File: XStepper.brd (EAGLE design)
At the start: 100.3 x 80 mm, 74 parts, among them Q2 16 MHZ

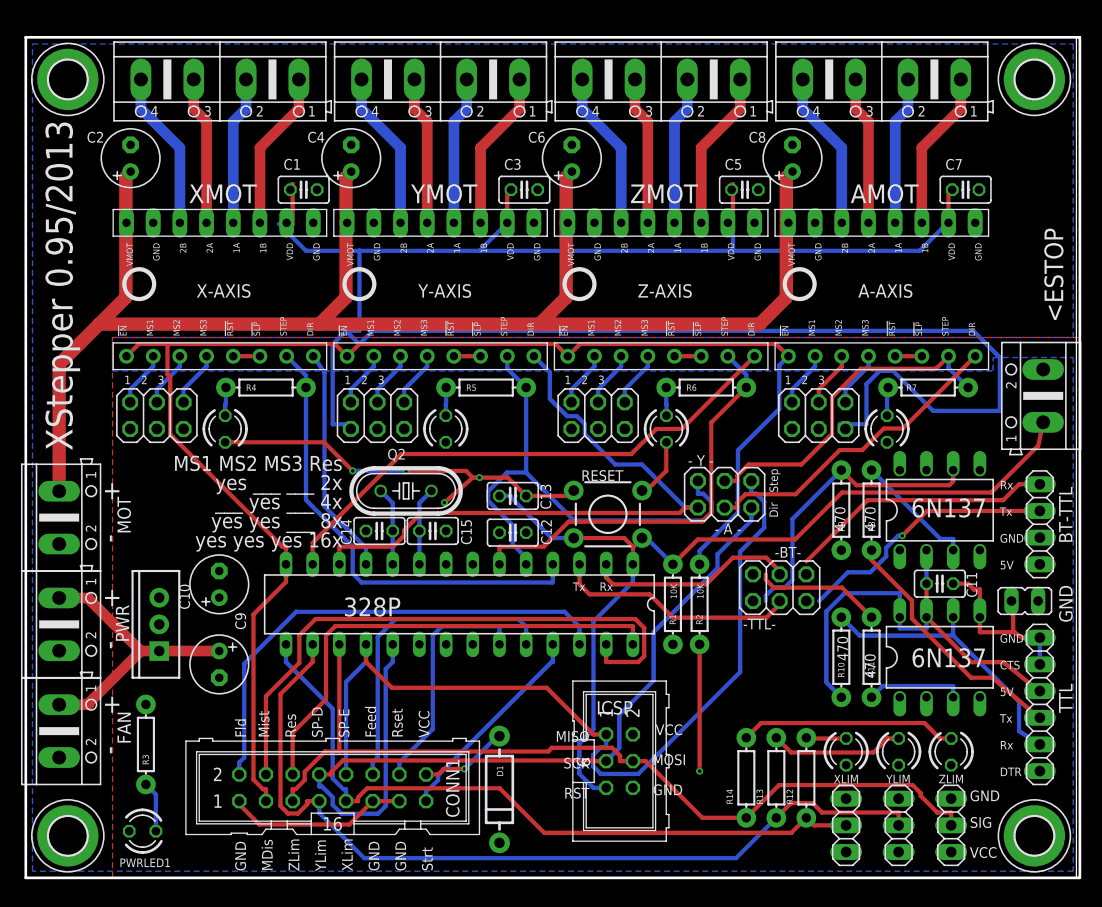
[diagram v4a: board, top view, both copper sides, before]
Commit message: - bugfix diode
- add new autorouting
- move emergency screw near to cpu
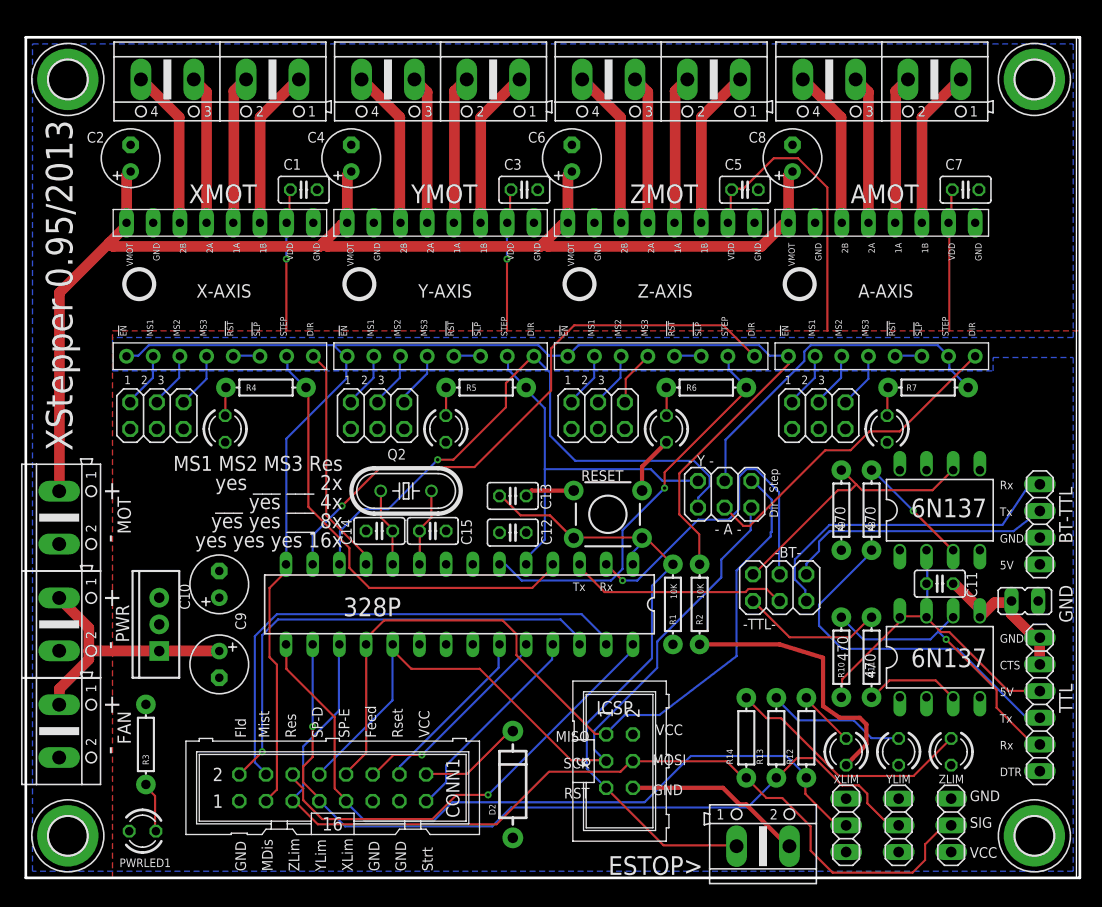
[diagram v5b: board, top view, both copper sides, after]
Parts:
- removed <ESTOP: (no value), con-ptr500:AK500/2
- removed D1: (no value), SparkFun-DiscreteSemi:DIODE-1N4001
- added D2: (no value), SparkFun-DiscreteSemi:DIODE-1N4001
- added ESTOP>: (no value), con-ptr500:AK500/2
- moved R12 3.81 mm to (74.3, 13.3)
- moved R13 3.81 mm to (71.4, 13.3)
- moved R14 3.81 mm to (68.6, 13.3)
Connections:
- net 5V: now also D2.A; no longer D1.C
- net GND: now also ESTOP>.2; no longer <ESTOP.2
- net N$45: now also D2.C; no longer D1.A
- net RESET: now also ESTOP>.1; no longer <ESTOP.1
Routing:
- net 5V: track 201.2 -> 69.5 mm, vias 0 -> 2
- net RESET: track 88.5 -> 62.3 mm
- net PWRMOT: track 144.0 -> 120.6 mm
- net GND: track 74.4 -> 53.2 mm, vias 5 -> 0
- net RXD: track 19.9 -> 32.1 mm, vias 0 -> 1
- net SPINDLE-DIR: track 82.8 -> 71.4 mm
- net Y-STEP: track 48.3 -> 37.1 mm
- net FEED-HOLD: track 30.1 -> 20.1 mm, vias 0 -> 1
- net USB_TXD: track 24.0 -> 33.9 mm
- net USB_5V: track 43.4 -> 33.5 mm
- net Z-STOP: track 82.9 -> 91.4 mm
- net COOLANT-MIST: track 56.6 -> 49.4 mm
- net G-RESET: track 23.0 -> 16.4 mm
- net BTTXD: track 25.3 -> 31.2 mm
- net SPINDLE-ENABLE: track 82.6 -> 77.2 mm
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
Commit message: - add VMOT sign to driver for users
- remove circle for pod cuz they are different on drivers
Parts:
- R12, R13, R14: value (none) -> 220
- R3: value (none) -> 330
- R4, R5, R6, R7: value (none) -> 110
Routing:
- net PWRMOT: track 120.6 -> 127.9 mm
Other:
- board text added: "VMOT>"
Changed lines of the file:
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@@
 <text x="52.07" y="27.305" size="0.8128" layer="25">Tx</text>
 <text x="54.61" y="27.305" size="0.8128" layer="25">Rx</text>
-<circle x="10.795" y="56.515" radius="1.419903125" width="0.4064" layer="25"/>
-<circle x="31.75" y="56.515" radius="1.419903125" width="0.4064" layer="25"/>
-<circle x="52.705" y="56.515" radius="1.419903125" width="0.4064" layer="25"/>
-<circle x="73.66" y="56.515" radius="1.419903125" width="0.4064" layer="25"/>
+<text x="8.89" y="55.245" size="1.27" layer="25" font="vector" rot="R90">VMOT&gt;</text>
+<text x="29.845" y="55.245" size="1.27" layer="25" font="vector" rot="R90">VMOT&gt;</text>
+<text x="50.8" y="55.245" size="1.27" layer="25" font="vector" rot="R90">VMOT&gt;</text>
+<text x="71.755" y="55.245" size="1.27" layer="25" font="vector" rot="R90">VMOT&gt;</text>
 </plain>
 <attributes>
@@
 </element>
 <element name="IC1" library="SparkFun-PowerIC" package="TO220-IGO" value="" x="12.7" y="24.13" rot="R90"/>
-<element name="R3" library="SparkFun-Resistors" package="AXIAL-0.3" value="" x="11.43" y="12.7" smashed="yes" rot="R270">
+<element name="R3" library="SparkFun-Resistors" package="AXIAL-0.3" value="330" x="11.43" y="12.7" smashed="yes" rot="R270">
 <attribute name="NAME" x="11.1125" y="11.7475" size="0.6096" layer="25" font="vector" rot="R270"/>
 <attribute name="VALUE" x="11.049" y="14.732" size="1.016" layer="21" font="vector" ratio="15" rot="R270"/>
@@
 <attribute name="VALUE" x="64.516" y="26.543" size="0.6096" layer="21" font="vector" ratio="15" rot="R90"/>
 </element>
-<element name="R4" library="SparkFun-Resistors" package="AXIAL-0.3" value="" x="22.8601" y="46.6725" smashed="yes">
+<element name="R4" library="SparkFun-Resistors" package="AXIAL-0.3" value="110" x="22.8601" y="46.6725" smashed="yes">
 <attribute name="NAME" x="20.9551" y="46.355" size="0.6096" layer="25" font="vector"/>
 <attribute name="VALUE" x="20.8281" y="46.2915" size="1.016" layer="21" font="vector" ratio="15"/>
 </element>
-<element name="R5" library="SparkFun-Resistors" package="AXIAL-0.3" value="" x="43.8151" y="46.6725" smashed="yes">
+<element name="R5" library="SparkFun-Resistors" package="AXIAL-0.3" value="110" x="43.8151" y="46.6725" smashed="yes">
 <attribute name="NAME" x="41.9101" y="46.355" size="0.6096" layer="25" font="vector"/>
 <attribute name="VALUE" x="41.7831" y="46.2915" size="1.016" layer="21" font="vector" ratio="15"/>
 </element>
-<element name="R6" library="SparkFun-Resistors" package="AXIAL-0.3" value="" x="64.7701" y="46.6725" smashed="yes">
+<element name="R6" library="SparkFun-Resistors" package="AXIAL-0.3" value="110" x="64.7701" y="46.6725" smashed="yes">
 <attribute name="NAME" x="62.8651" y="46.355" size="0.6096" layer="25" font="vector"/>
 <attribute name="VALUE" x="62.7381" y="46.2915" size="1.016" layer="21" font="vector" ratio="15"/>
 </element>
-<element name="R7" library="SparkFun-Resistors" package="AXIAL-0.3" value="" x="85.8838" y="46.6725" smashed="yes">
+<element name="R7" library="SparkFun-Resistors" package="AXIAL-0.3" value="110" x="85.8838" y="46.6725" smashed="yes">
 <attribute name="NAME" x="83.82005" y="46.355" size="0.6096" layer="25" font="vector"/>
 <attribute name="VALUE" x="83.8518" y="46.2915" size="1.016" layer="21" font="vector" ratio="15"/>
 </element>
-<element name="R12" library="SparkFun-Resistors" package="AXIAL-0.3" value="" x="74.295" y="13.335" smashed="yes" rot="R90">
+<element name="R12" library="SparkFun-Resistors" package="AXIAL-0.3" value="220" x="74.295" y="13.335" smashed="yes" rot="R90">
 <attribute name="NAME" x="73.025" y="10.795" size="0.6096" layer="25" font="vector" rot="R90"/>
 <attribute name="VALUE" x="74.676" y="11.303" size="1.016" layer="21" font="vector" ratio="15" rot="R90"/>
 </element>
-<element name="R13" library="SparkFun-Resistors" package="AXIAL-0.3" value="" x="71.4375" y="13.335" smashed="yes" rot="R90">
+<element name="R13" library="SparkFun-Resistors" package="AXIAL-0.3" value="220" x="71.4375" y="13.335" smashed="yes" rot="R90">
 <attribute name="NAME" x="70.1675" y="10.795" size="0.6096" layer="25" font="vector" rot="R90"/>
 <attribute name="VALUE" x="71.8185" y="11.303" size="1.016" layer="21" font="vector" ratio="15" rot="R90"/>
 </element>
-<element name="R14" library="SparkFun-Resistors" package="AXIAL-0.3" value="" x="68.58" y="13.335" smashed="yes" rot="R90">
+<element name="R14" library="SparkFun-Resistors" package="AXIAL-0.3" value="220" x="68.58" y="13.335" smashed="yes" rot="R90">
 <attribute name="NAME" x="67.31" y="10.795" size="0.6096" layer="25" font="vector" rot="R90"/>
 <attribute name="VALUE" x="68.961" y="11.303" size="1.016" layer="21" font="vector" ratio="15" rot="R90"/>
@@
 <wire x1="67.945" y1="6.985" x2="68.58" y2="6.985" width="0.4064" layer="1"/>
 <wire x1="68.58" y1="6.985" x2="72.39" y2="3.175" width="0.4064" layer="1"/>
-<wire x1="64.135" y1="22.225" x2="71.755" y2="22.225" width="0.4064" layer="1"/>
+<wire x1="64.135" y1="22.225" x2="65.405" y2="20.955" width="0.4064" layer="1"/>
 <wire x1="78.08" y1="10.73" x2="80.01" y2="12.7" width="0.4064" layer="1"/>
 <wire x1="80.01" y1="12.7" x2="80.01" y2="14.605" width="0.4064" layer="1"/>
 <wire x1="80.01" y1="14.605" x2="79.375" y2="15.24" width="0.4064" layer="1"/>
-<wire x1="79.375" y1="15.24" x2="77.47" y2="15.24" width="0.4064" layer="1"/>
-<wire x1="77.47" y1="15.24" x2="75.8825" y2="16.35125" width="0.4064" layer="1"/>
+<wire x1="79.375" y1="15.24" x2="76.99375" y2="15.24" width="0.4064" layer="1"/>
+<wire x1="76.99375" y1="15.24" x2="75.8825" y2="16.35125" width="0.4064" layer="1"/>
 <wire x1="75.8825" y1="16.35125" x2="75.8825" y2="20.955" width="0.4064" layer="1"/>
-<wire x1="75.8825" y1="20.955" x2="71.755" y2="22.225" width="0.4064" layer="1"/>
+<wire x1="75.8825" y1="20.955" x2="65.405" y2="20.955" width="0.4064" layer="1"/>
 </signal>
 <signal name="N$5">
@@
 <wire x1="25.1" y1="65.5" x2="25.1825" y2="65.5" width="0.2032" layer="1"/>
 <wire x1="24.9" y1="62.4" x2="24.8263" y2="62.35" width="0.2032" layer="1"/>
-<wire x1="24.8" y1="58.9" x2="24.8" y2="62.3" width="0.2032" layer="16"/>
-<wire x1="24.8" y1="52.07" x2="24.8" y2="58.9" width="0.2032" layer="1"/>
+<wire x1="24.8" y1="55.725" x2="24.8" y2="62.3" width="0.2032" layer="16"/>
+<wire x1="24.8" y1="52.07" x2="24.8" y2="55.725" width="0.2032" layer="1"/>
 <wire x1="24.8" y1="62.3" x2="24.8263" y2="62.35" width="0.2032" layer="16"/>
-<wire x1="45.8" y1="58.9" x2="45.8" y2="62.3" width="0.2032" layer="16"/>
-<wire x1="45.8" y1="52.07" x2="45.8" y2="58.9" width="0.2032" layer="1"/>
+<wire x1="45.8" y1="55.725" x2="45.8" y2="62.3" width="0.2032" layer="16"/>
+<wire x1="45.8" y1="52.07" x2="45.8" y2="55.725" width="0.2032" layer="1"/>
 <wire x1="45.8" y1="62.3" x2="45.8263" y2="62.35" width="0.2032" layer="16"/>
 <wire x1="68.3" y1="65.6" x2="67.2" y2="65.6" width="0.2032" layer="1"/>
@@
 <wire x1="87.9" y1="52.07" x2="87.9" y2="62.3" width="0.2032" layer="1"/>
 <wire x1="87.9" y1="62.3" x2="87.8262" y2="62.35" width="0.2032" layer="1"/>
-<via x="24.8" y="58.9" extent="1-16" drill="0.3302"/>
-<via x="45.8" y="58.9" extent="1-16" drill="0.3302"/>
+<via x="24.8" y="55.725" extent="1-16" drill="0.3302"/>
+<via x="45.8" y="55.725" extent="1-16" drill="0.3302"/>
 <wire x1="77.6" y1="31.2" x2="77.625" y2="31.19" width="0.2032" layer="1"/>
 </signal>
@@
 <wire x1="9.9" y1="67.2" x2="9.9763" y2="67.23" width="1.016" layer="1"/>
 <wire x1="3.2" y1="55.7" x2="3.2" y2="36.9" width="1.016" layer="1"/>
-<wire x1="9.4" y1="61.9" x2="7.95" y2="60.45" width="1.016" layer="1"/>
-<wire x1="7.95" y1="60.45" x2="3.2" y2="55.7" width="1.016" layer="1"/>
+<wire x1="9.4" y1="61.9" x2="6.045" y2="58.545" width="1.016" layer="1"/>
+<wire x1="6.045" y1="58.545" x2="3.2" y2="55.7" width="1.016" layer="1"/>
 <wire x1="3.2" y1="36.9" x2="3.175" y2="36.8046" width="1.016" layer="1"/>
 <wire x1="9.4" y1="61.9" x2="9.5863" y2="62.35" width="1.016" layer="1"/>
-<wire x1="28" y1="60.1" x2="28.35" y2="60.45" width="1.016" layer="1"/>
-<wire x1="28.35" y1="60.45" x2="30.1" y2="62.2" width="1.016" layer="1"/>
-<wire x1="8.3" y1="60.1" x2="28" y2="60.1" width="1.016" layer="1"/>
+<wire x1="27.52375" y1="58.195" x2="27.55625" y2="58.2275" width="1.016" layer="1"/>
+<wire x1="27.55625" y1="58.2275" x2="30.1" y2="62.2" width="1.016" layer="1"/>
+<wire x1="7.03" y1="58.195" x2="27.52375" y2="58.195" width="1.016" layer="1"/>
 <wire x1="30.1" y1="62.2" x2="30.5863" y2="62.35" width="1.016" layer="1"/>
-<wire x1="8.3" y1="60.1" x2="7.95" y2="60.45" width="1.016" layer="1"/>
-<wire x1="49" y1="60.1" x2="49.35" y2="60.45" width="1.016" layer="1"/>
-<wire x1="49.35" y1="60.45" x2="51.1" y2="62.2" width="1.016" layer="1"/>
-<wire x1="28.7" y1="60.1" x2="49" y2="60.1" width="1.016" layer="1"/>
+<wire x1="7.03" y1="58.195" x2="6.045" y2="58.545" width="1.016" layer="1"/>
+<wire x1="48.365" y1="58.195" x2="48.715" y2="58.545" width="1.016" layer="1"/>
+<wire x1="48.715" y1="58.545" x2="51.1" y2="62.2" width="1.016" layer="1"/>
+<wire x1="28.7" y1="58.195" x2="48.365" y2="58.195" width="1.016" layer="1"/>
 <wire x1="51.1" y1="62.2" x2="51.5863" y2="62.35" width="1.016" layer="1"/>
-<wire x1="28.7" y1="60.1" x2="28.35" y2="60.45" width="1.016" layer="1"/>
-<wire x1="70" y1="60.1" x2="72.1" y2="62.2" width="1.016" layer="1"/>
-<wire x1="49.7" y1="60.1" x2="70" y2="60.1" width="1.016" layer="1"/>
+<wire x1="28.7" y1="58.195" x2="27.55625" y2="58.2275" width="1.016" layer="1"/>
+<wire x1="68.73" y1="58.195" x2="72.1" y2="62.2" width="1.016" layer="1"/>
+<wire x1="48.43" y1="58.195" x2="68.73" y2="58.195" width="1.016" layer="1"/>
 <wire x1="72.1" y1="62.2" x2="72.5862" y2="62.35" width="1.016" layer="1"/>
-<wire x1="49.7" y1="60.1" x2="49.35" y2="60.45" width="1.016" layer="1"/>
+<wire x1="48.43" y1="58.195" x2="48.715" y2="58.545" width="1.016" layer="1"/>
 </signal>
 <signal name="N$43">

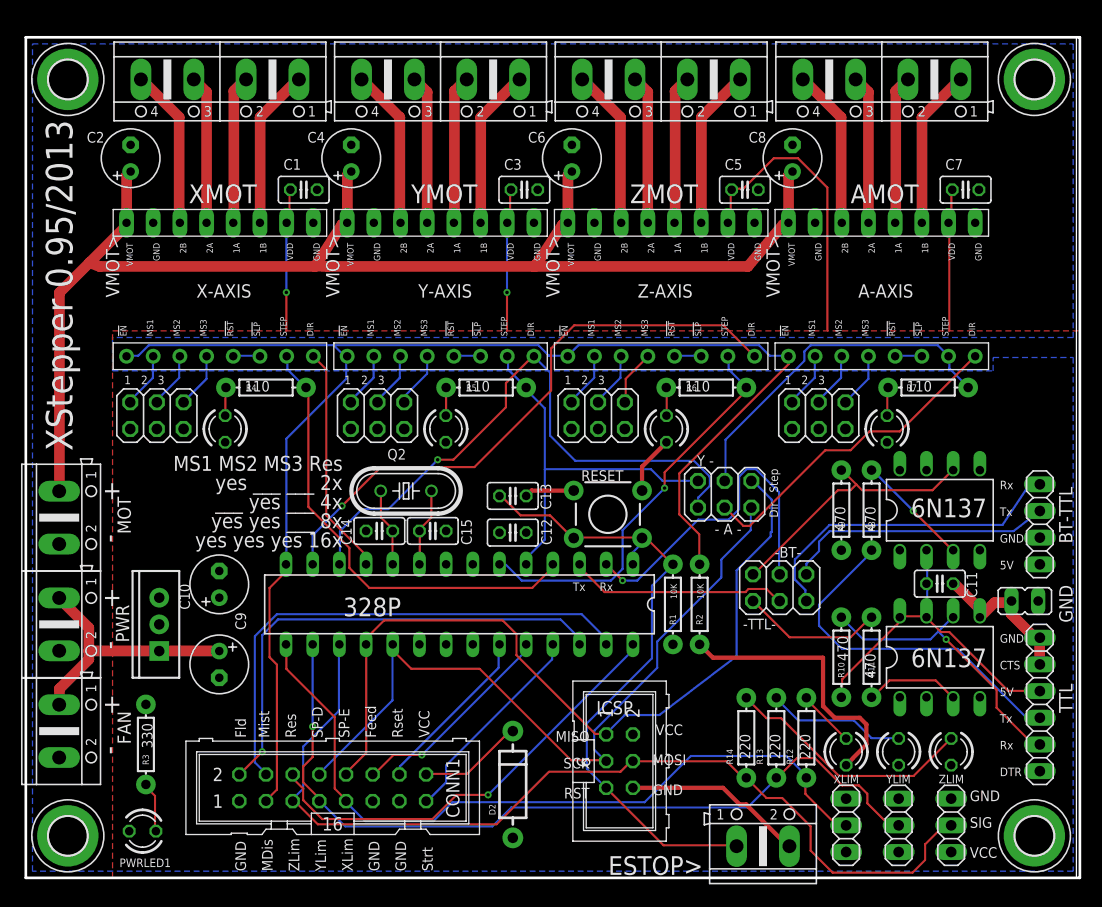
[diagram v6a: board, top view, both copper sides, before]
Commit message: - some changes for community
* move screw terminals for motors 1mm up for bigger caps
* add a 12V voltage regulator for fan
* replace powerled resitor to a small one
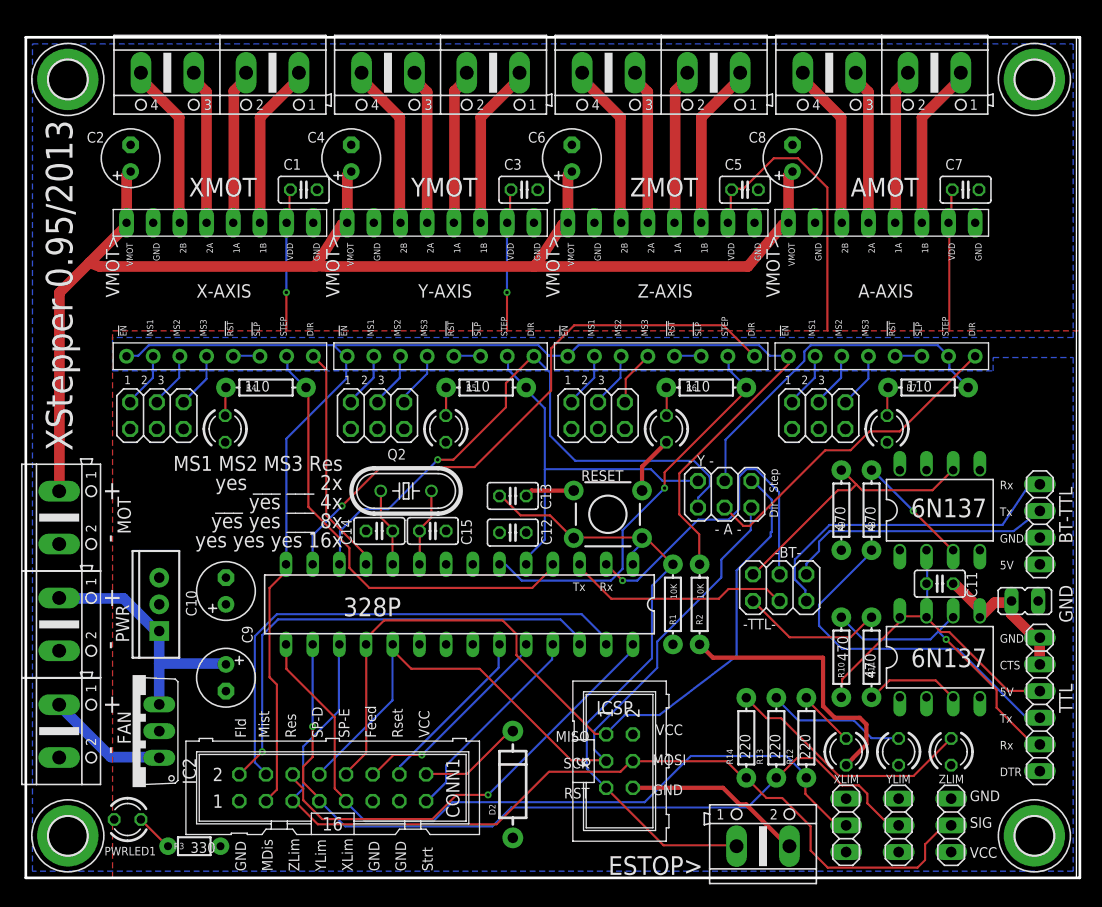
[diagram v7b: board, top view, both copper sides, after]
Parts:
- added IC2: 7812TV, linear:TO220V
- R3: device SparkFun-Resistors:AXIAL-0.3 -> SparkFun-Resistors:1/6W-RES
- moved R3 10.7 mm to (16.0, 3.02), turned to 180 degrees
- moved IC1 1.91 mm to (12.7, 26.0)
- moved PWRLED1 1.81 mm to (9.68, 5.56)
- moved C9 1.42 mm to (19.1, 19.1)
- moved C10 0.90 mm to (19.1, 27.3)
- moved AMOT 0.64 mm to (81.5, 76.6)
- moved XMOT 0.64 mm to (18.5, 76.6)
- moved YMOT 0.64 mm to (39.5, 76.6)
- moved ZMOT 0.64 mm to (60.5, 76.6)
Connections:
- new net N$46: FAN.1, IC2.1
- net 12V: now also IC2.3; no longer FAN.1
- net 5V: now also R3.1; no longer R3.P$1
- net GND: now also IC2.2
- net N$43: now also R3.2; no longer R3.P$2
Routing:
- net N$46: track 0.00 -> 11.7 mm
- net N$43: track 4.84 -> 3.65 mm
- net 12V: track 24.9 -> 24.2 mm
- net N$3: track 14.2 -> 14.8 mm
- net N$18: track 14.2 -> 14.8 mm
- net N$11: track 14.2 -> 14.8 mm
- net N$27: track 14.2 -> 14.8 mm
- net N$4: track 15.2 -> 15.8 mm
- net N$17: track 15.2 -> 15.8 mm
- net N$12: track 15.2 -> 15.8 mm
- net N$28: track 15.2 -> 15.8 mm
- net N$26: track 14.2 -> 14.8 mm
- net N$2: track 14.2 -> 14.8 mm
- net N$19: track 14.2 -> 14.8 mm
- net N$10: track 14.2 -> 14.8 mm
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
